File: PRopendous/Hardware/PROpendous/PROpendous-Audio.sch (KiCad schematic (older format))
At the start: 30 parts, among them IC7 MMA7455, M1 ELECTRET_MIC, U7 Video, U8 Headphones, U9 Line

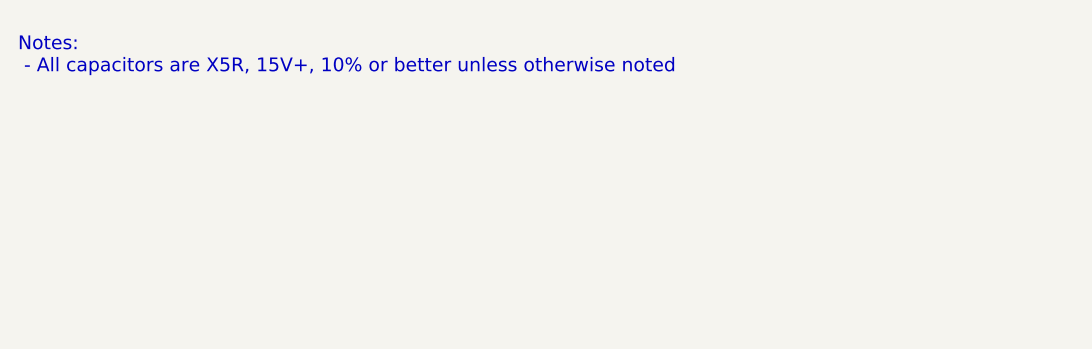
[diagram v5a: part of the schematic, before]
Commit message: Updated design files.  Added picture of finished PCB.
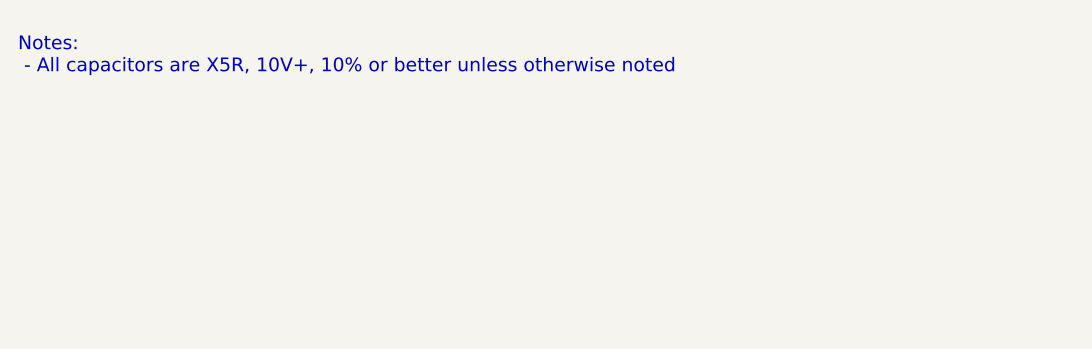
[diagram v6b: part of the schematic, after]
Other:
- note added: "Notes:\n - All capacitors are X5R, 10V+, 10% or better unless otherwise noted"
- note removed: "Notes:\n - All capacitors are X5R, 15V+, 10% or better unless otherwise noted"
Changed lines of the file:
@@
-EESchema Schematic File Version 2  date 27/04/2010 18:25:33
+EESchema Schematic File Version 2  date 07/05/2010 11:28:22
 LIBS:opendous
 LIBS:device
@@
 LIBS:valves
 LIBS:power
-LIBS:PROpendous-cache
 EELAYER 24  0
 EELAYER END
@@
 Sheet 6 8
 Title "PROpendous"
-Date "27 apr 2010"
+Date "7 may 2010"
 Rev "1.0"
 Comp "Opendous Inc. (www.opendous.org)"
@@
 $EndComp
 Text Notes 650  750  0    60   ~ 0
-Notes:\n - All capacitors are X5R, 15V+, 10% or better unless otherwise noted
+Notes:\n - All capacitors are X5R, 10V+, 10% or better unless otherwise noted
 Text GLabel 6450 3450 2    40   BiDi ~ 0
 MIC
